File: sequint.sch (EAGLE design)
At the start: 66 parts, among them IC1 STM32F10XCXT6, Q1 MOSFET-NCHANNELSMD, Q2 MOSFET-NCHANNELSMD, Q3 MOSFET-NCHANNELSMD, Q4 MOSFET-NCHANNELSMD, Q5 16MHz, U1 LSM330DLCTRLGA, U2 MCP73831, U4 NRF24L01SMD

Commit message: s/trace antenna/chip antenna/, passes DRC.
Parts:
- removed ANT1: ANTENNA, adafruit:ANTENNA
- added U$1: ANTENNA2SMD5, SparkFun-RF:ANTENNA2SMD5
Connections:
- net ANT: now also U$1.SIGNAL; no longer ANT1.FEED
- net GND: no longer ANT1.GND
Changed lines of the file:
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@@
 <part name="GND7" library="SparkFun" deviceset="GND" device=""/>
 <part name="U4" library="SparkFun" deviceset="NRF24L01" device="SMD"/>
-<part name="ANT1" library="adafruit" deviceset="ANTENNA" device=""/>
 <part name="JPRF-A" library="nonolith" deviceset="HEADER-1X4" device="ROUND"/>
 <part name="JPRF-B" library="nonolith" deviceset="HEADER-1X4" device="ROUND"/>
@@
 <part name="R10" library="nonolith" deviceset="RESISTOR" device="0603" value="130o"/>
 <part name="JP1" library="nonolith" deviceset="HEADER-1X4" device="ROUND" value="PORTC"/>
+<part name="U$1" library="SparkFun-RF" deviceset="ANTENNA2" device="SMD5"/>
 </parts>
 <sheets>
@@
 <attribute name="VALUE" x="45.466" y="72.136" size="1.6764" layer="96"/>
 </instance>
-<instance part="ANT1" gate="G$1" x="111.76" y="88.9"/>
 <instance part="JPRF-A" gate="A" x="-10.16" y="78.74"/>
 <instance part="JPRF-B" gate="A" x="-7.62" y="81.28" rot="R180"/>
@@
 <instance part="C18" gate="G$1" x="96.52" y="22.86"/>
 <instance part="C19" gate="G$1" x="106.68" y="22.86"/>
+<instance part="U$1" gate="G$1" x="111.76" y="88.9"/>
 </instances>
 <busses>
@@
 <pinref part="C13" gate="G$1" pin="P$1"/>
 <pinref part="GND7" gate="1" pin="GND"/>
-<pinref part="ANT1" gate="G$1" pin="GND"/>
-<wire x1="114.3" y1="88.9" x2="114.3" y2="71.12" width="0" layer="91"/>
-<wire x1="114.3" y1="71.12" x2="101.6" y2="71.12" width="0" layer="91"/>
 </segment>
 <segment>
@@
 <wire x1="101.6" y1="81.28" x2="101.6" y2="83.82" width="0" layer="91"/>
 <wire x1="101.6" y1="83.82" x2="111.76" y2="83.82" width="0" layer="91"/>
-<wire x1="111.76" y1="83.82" x2="111.76" y2="88.9" width="0" layer="91"/>
 <junction x="101.6" y="83.82"/>
 <label x="104.14" y="83.82" size="1.778" layer="95"/>
 <pinref part="C14" gate="G$1" pin="P$2"/>
 <pinref part="C13" gate="G$1" pin="P$2"/>
-<pinref part="ANT1" gate="G$1" pin="FEED"/>
-</segment>
-</net>
+<pinref part="U$1" gate="G$1" pin="SIGNAL"/>
+</segment>
+</net>

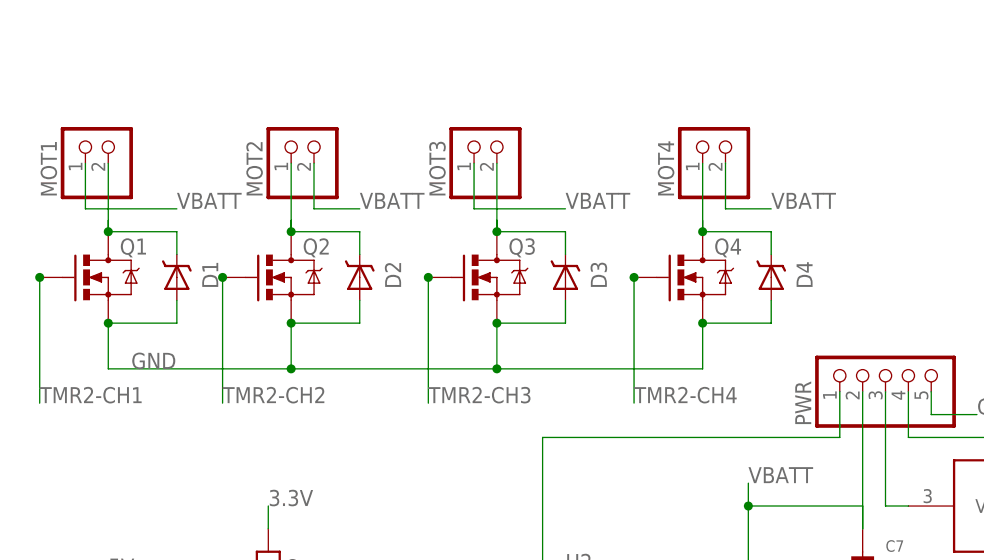
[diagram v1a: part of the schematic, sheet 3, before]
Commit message: removed fatty diodes, s/0603/0402/
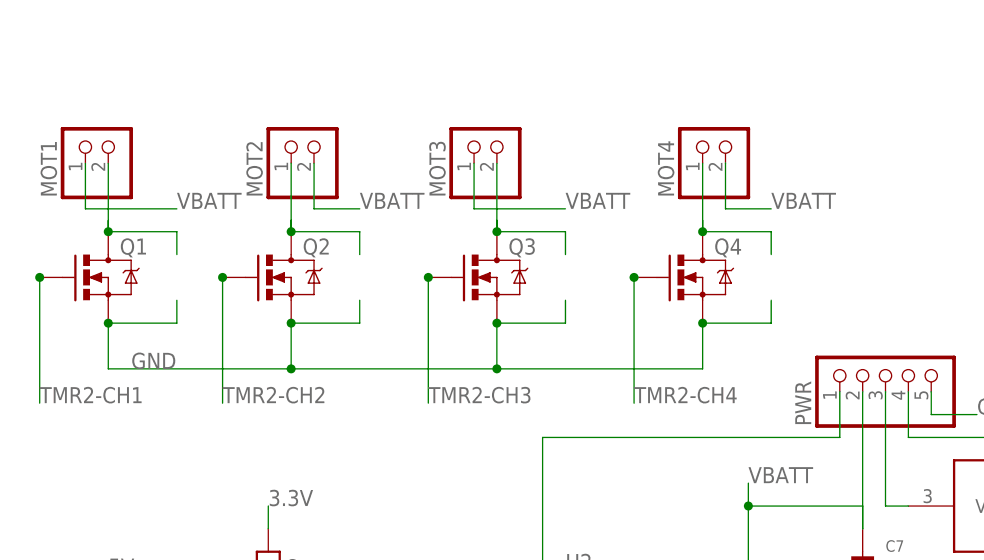
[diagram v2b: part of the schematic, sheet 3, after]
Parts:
- removed D1, D2, D3, D4: SCHOTTKY, nonolith:SCHOTTKY
- C1, C10, C11, C12, C13, C14, C15, C16, C17, C18, C19, C2, C21, C22, C3, C4, C5, C6, C8, C9: device nonolith:CAP_CERAMIC0603 -> nonolith:CAP_CERAMIC0402
- C20: device nonolith:CAP_CERAMIC1206 -> nonolith:CAP_CERAMIC0402
- L1, L2, L3: device SparkFun:INDUCTOR0603 -> SparkFun:INDUCTOR0402
- R1, R10, R2, R3, R4, R5, R6, R7, R8, R9: device nonolith:RESISTOR0603 -> nonolith:RESISTOR0402
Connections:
- net GND: no longer D1.A, D2.A, D3.A, D4.A
- net VL-1: no longer D1.C
- net VL-2: no longer D2.C
- net VL-3: no longer D3.C
- net VL-4: no longer D4.C

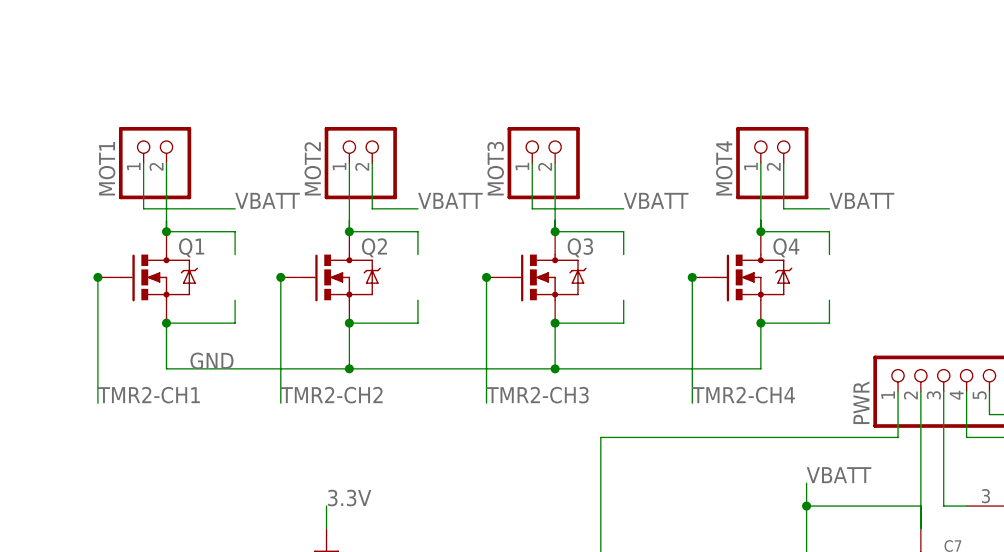
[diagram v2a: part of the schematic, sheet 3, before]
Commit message: added snubber diodes in SOD523 aka tiny
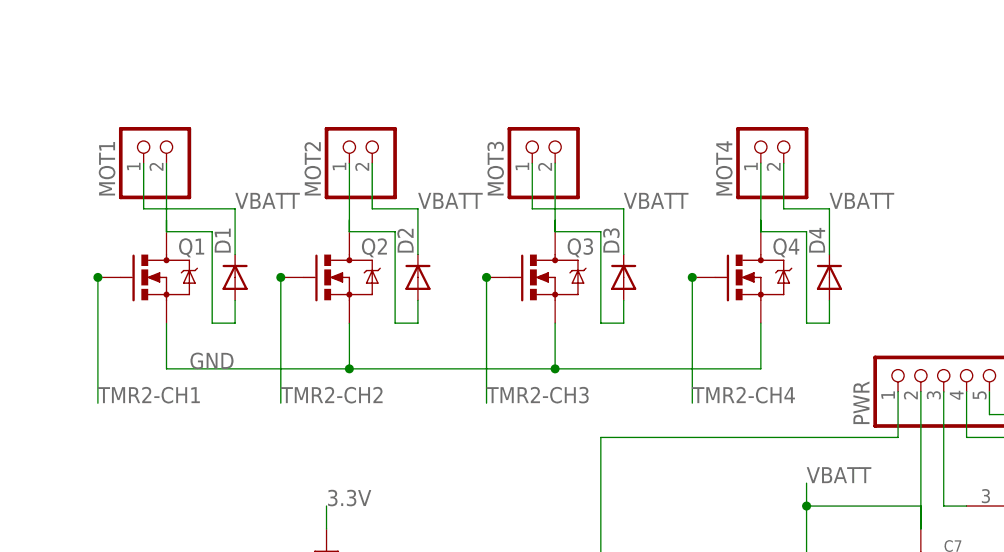
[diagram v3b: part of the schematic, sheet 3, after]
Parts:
- added D1, D2, D3, D4: (no value), SparkFun-DiscreteSemi:DIODESOD523
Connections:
- net VBATT: now also D1.C, D2.C, D3.C, D4.C
- net VL-1: now also D1.A
- net VL-2: now also D2.A
- net VL-3: now also D3.A
- net VL-4: now also D4.A
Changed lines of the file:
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@@
 <part name="JP1" library="nonolith" deviceset="HEADER-1X4" device="ROUND" value="PORTC"/>
 <part name="U$1" library="SparkFun-RF" deviceset="ANTENNA2" device="SMD5"/>
+<part name="D1" library="SparkFun-DiscreteSemi" deviceset="DIODE" device="SOD523"/>
+<part name="D2" library="SparkFun-DiscreteSemi" deviceset="DIODE" device="SOD523"/>
+<part name="D3" library="SparkFun-DiscreteSemi" deviceset="DIODE" device="SOD523"/>
+<part name="D4" library="SparkFun-DiscreteSemi" deviceset="DIODE" device="SOD523"/>
 </parts>
 <sheets>
@@
 <instance part="RN1" gate="C" x="149.86" y="66.04" rot="R90"/>
 <instance part="RN1" gate="D" x="149.86" y="50.8" rot="R90"/>
+<instance part="D1" gate="G$1" x="30.48" y="48.26" rot="R90"/>
+<instance part="D2" gate="G$1" x="50.8" y="48.26" rot="R90"/>
+<instance part="D3" gate="G$1" x="73.66" y="48.26" rot="R90"/>
+<instance part="D4" gate="G$1" x="96.52" y="48.26" rot="R90"/>
 </instances>
 <busses>
@@
 <segment>
 <pinref part="Q4" gate="G$1" pin="D"/>
-<wire x1="96.52" y1="50.8" x2="96.52" y2="53.34" width="0" layer="91"/>
-<wire x1="96.52" y1="53.34" x2="88.9" y2="53.34" width="0" layer="91"/>
 <wire x1="88.9" y1="53.34" x2="88.9" y2="54.61" width="0" layer="91"/>
-<junction x="88.9" y="53.34"/>
 <pinref part="MOT4" gate="G$1" pin="1"/>
 <wire x1="88.9" y1="53.34" x2="88.9" y2="60.96" width="0" layer="91"/>
+<wire x1="88.9" y1="53.34" x2="93.98" y2="53.34" width="0" layer="91"/>
+<wire x1="93.98" y1="53.34" x2="93.98" y2="43.18" width="0" layer="91"/>
+<pinref part="D4" gate="G$1" pin="A"/>
+<wire x1="96.52" y1="45.72" x2="96.52" y2="43.18" width="0" layer="91"/>
+<wire x1="93.98" y1="43.18" x2="96.52" y2="43.18" width="0" layer="91"/>
 </segment>
 </net>
@@
 <segment>
 <pinref part="Q3" gate="G$1" pin="D"/>
-<wire x1="73.66" y1="50.8" x2="73.66" y2="53.34" width="0" layer="91"/>
-<wire x1="73.66" y1="53.34" x2="66.04" y2="53.34" width="0" layer="91"/>
 <wire x1="66.04" y1="53.34" x2="66.04" y2="54.61" width="0" layer="91"/>
-<junction x="66.04" y="53.34"/>
 <pinref part="MOT3" gate="G$1" pin="2"/>
 <wire x1="66.04" y1="60.96" x2="66.04" y2="53.34" width="0" layer="91"/>
+<wire x1="66.04" y1="53.34" x2="71.12" y2="53.34" width="0" layer="91"/>
+<wire x1="71.12" y1="53.34" x2="71.12" y2="43.18" width="0" layer="91"/>
+<pinref part="D3" gate="G$1" pin="A"/>
+<wire x1="73.66" y1="45.72" x2="73.66" y2="43.18" width="0" layer="91"/>
+<wire x1="71.12" y1="43.18" x2="73.66" y2="43.18" width="0" layer="91"/>
 </segment>
 </net>
@@
 <segment>
 <pinref part="Q2" gate="G$1" pin="D"/>
-<wire x1="50.8" y1="50.8" x2="50.8" y2="53.34" width="0" layer="91"/>
-<wire x1="50.8" y1="53.34" x2="43.18" y2="53.34" width="0" layer="91"/>
 <wire x1="43.18" y1="53.34" x2="43.18" y2="54.61" width="0" layer="91"/>
-<junction x="43.18" y="53.34"/>
 <pinref part="MOT2" gate="G$1" pin="1"/>
 <wire x1="43.18" y1="60.96" x2="43.18" y2="53.34" width="0" layer="91"/>
+<wire x1="43.18" y1="53.34" x2="48.26" y2="53.34" width="0" layer="91"/>
+<wire x1="48.26" y1="53.34" x2="48.26" y2="43.18" width="0" layer="91"/>
+<pinref part="D2" gate="G$1" pin="A"/>
+<wire x1="50.8" y1="45.72" x2="50.8" y2="43.18" width="0" layer="91"/>
+<wire x1="48.26" y1="43.18" x2="50.8" y2="43.18" width="0" layer="91"/>
 </segment>
 </net>
@@
 <segment>
 <pinref part="Q1" gate="G$1" pin="D"/>
-<wire x1="30.48" y1="50.8" x2="30.48" y2="53.34" width="0" layer="91"/>
-<wire x1="30.48" y1="53.34" x2="22.86" y2="53.34" width="0" layer="91"/>
 <wire x1="22.86" y1="53.34" x2="22.86" y2="54.61" width="0" layer="91"/>
-<junction x="22.86" y="53.34"/>
 <pinref part="MOT1" gate="G$1" pin="2"/>
 <wire x1="22.86" y1="53.34" x2="22.86" y2="60.96" width="0" layer="91"/>
+<wire x1="22.86" y1="53.34" x2="27.94" y2="53.34" width="0" layer="91"/>
+<wire x1="27.94" y1="53.34" x2="27.94" y2="43.18" width="0" layer="91"/>
+<pinref part="D1" gate="G$1" pin="A"/>
+<wire x1="30.48" y1="45.72" x2="30.48" y2="43.18" width="0" layer="91"/>
+<wire x1="27.94" y1="43.18" x2="30.48" y2="43.18" width="0" layer="91"/>
 </segment>
 </net>
@@
 <wire x1="66.04" y1="38.1" x2="88.9" y2="38.1" width="0" layer="91"/>
 <wire x1="88.9" y1="38.1" x2="88.9" y2="43.18" width="0" layer="91"/>
-<wire x1="30.48" y1="45.72" x2="30.48" y2="43.18" width="0" layer="91"/>
-<wire x1="30.48" y1="43.18" x2="22.86" y2="43.18" width="0" layer="91"/>
-<wire x1="50.8" y1="45.72" x2="50.8" y2="43.18" width="0" layer="91"/>
-<wire x1="50.8" y1="43.18" x2="43.18" y2="43.18" width="0" layer="91"/>
-<wire x1="73.66" y1="45.72" x2="73.66" y2="43.18" width="0" layer="91"/>
-<wire x1="73.66" y1="43.18" x2="66.04" y2="43.18" width="0" layer="91"/>
-<wire x1="96.52" y1="45.72" x2="96.52" y2="43.18" width="0" layer="91"/>
-<wire x1="96.52" y1="43.18" x2="88.9" y2="43.18" width="0" layer="91"/>
-<junction x="22.86" y="43.18"/>
-<junction x="43.18" y="43.18"/>
-<junction x="66.04" y="43.18"/>
-<junction x="88.9" y="43.18"/>
 <junction x="66.04" y="38.1"/>
 <junction x="43.18" y="38.1"/>
@@
 <label x="30.48" y="55.88" size="1.778" layer="95"/>
 <pinref part="MOT1" gate="G$1" pin="1"/>
+<wire x1="30.48" y1="50.8" x2="30.48" y2="55.88" width="0" layer="91"/>
 <wire x1="30.48" y1="55.88" x2="20.32" y2="55.88" width="0" layer="91"/>
 <wire x1="20.32" y1="55.88" x2="20.32" y2="60.96" width="0" layer="91"/>
+<pinref part="D1" gate="G$1" pin="C"/>
 </segment>
 <segment>
@@
 <wire x1="45.72" y1="55.88" x2="50.8" y2="55.88" width="0" layer="91"/>
 <label x="50.8" y="55.88" size="1.778" layer="95"/>
+<pinref part="D2" gate="G$1" pin="C"/>
+<wire x1="50.8" y1="50.8" x2="50.8" y2="55.88" width="0" layer="91"/>
 </segment>
 <segment>
 <label x="73.66" y="55.88" size="1.778" layer="95"/>
 <pinref part="MOT3" gate="G$1" pin="1"/>
+<wire x1="73.66" y1="50.8" x2="73.66" y2="55.88" width="0" layer="91"/>
 <wire x1="73.66" y1="55.88" x2="63.5" y2="55.88" width="0" layer="91"/>
 <wire x1="63.5" y1="55.88" x2="63.5" y2="60.96" width="0" layer="91"/>
+<pinref part="D3" gate="G$1" pin="C"/>
 </segment>
 <segment>
@@
 <wire x1="91.44" y1="55.88" x2="96.52" y2="55.88" width="0" layer="91"/>
 <label x="96.52" y="55.88" size="1.778" layer="95"/>
-</segment>
-<segment>
+<pinref part="D4" gate="G$1" pin="C"/>
+<wire x1="96.52" y1="50.8" x2="96.52" y2="55.88" width="0" layer="91"/>
+</segment>
+<segment>

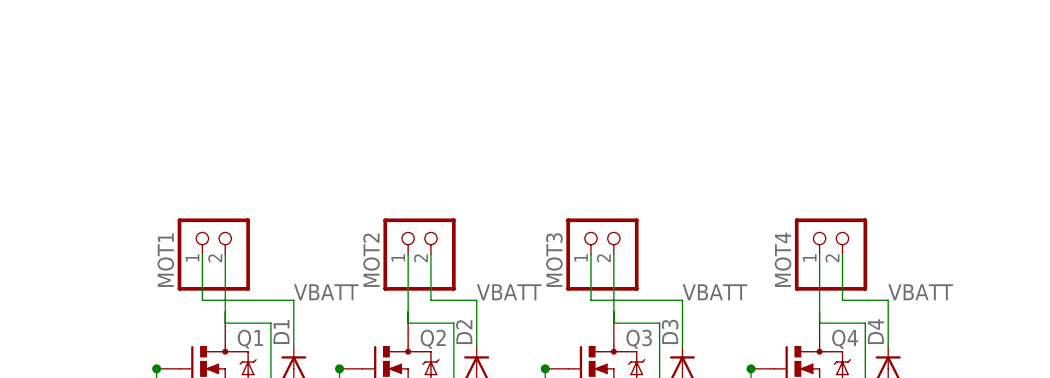
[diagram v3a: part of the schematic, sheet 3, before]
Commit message: Add servo headers
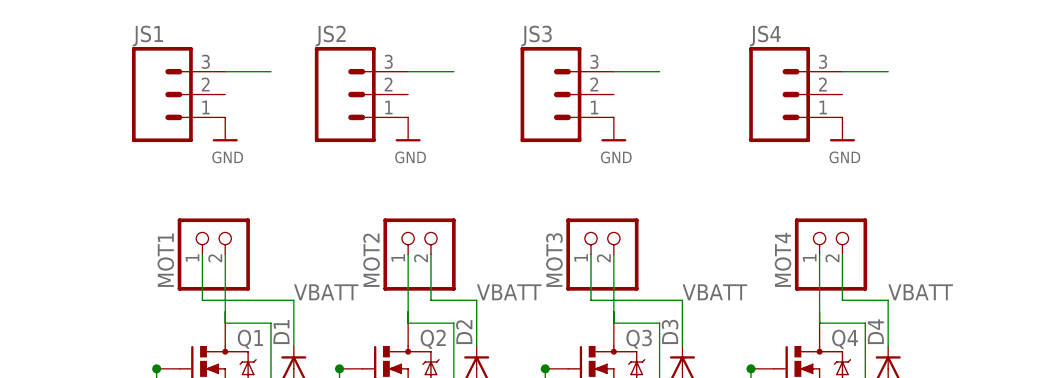
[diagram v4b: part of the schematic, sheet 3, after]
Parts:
- added JS1, JS2, JS3, JS4: (no value), SparkFun:M03LOCK
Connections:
- net GND: now also JS1.1, JS2.1, JS3.1, JS4.1
- net TMR2-CH1: now also JS1.3
- net TMR2-CH2: now also JS2.3
- net TMR2-CH3: now also JS3.3
- net TMR2-CH4: now also JS4.3

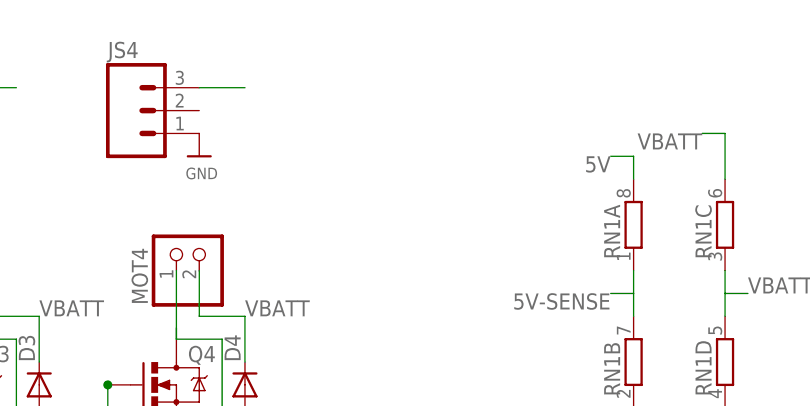
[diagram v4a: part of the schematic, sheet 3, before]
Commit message: Add test motor footprint
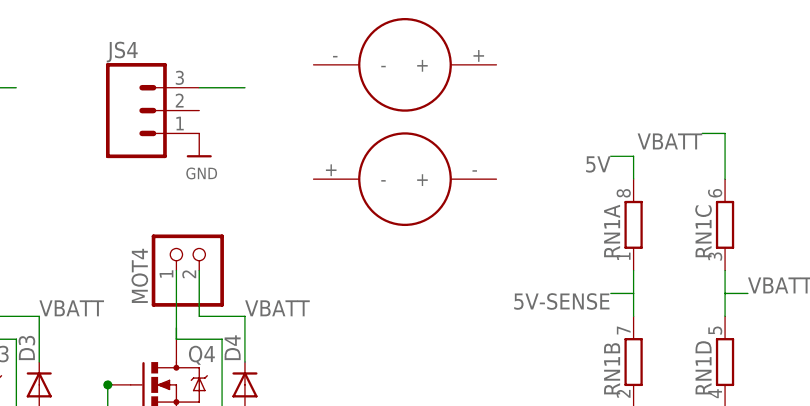
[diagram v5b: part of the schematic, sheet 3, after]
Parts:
- added U$6: MOT_RICCW, nonolith:MOT_RICCW
- added U$7: MOT_RICCCW, nonolith:MOT_RICCCW
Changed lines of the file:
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@@
 <part name="U$4" library="nonolith" deviceset="GND" device=""/>
 <part name="U$5" library="nonolith" deviceset="GND" device=""/>
+<part name="U$6" library="nonolith" deviceset="MOT_RIC" device="CW"/>
+<part name="U$7" library="nonolith" deviceset="MOT_RIC" device="CCW"/>
 </parts>
 <sheets>
@@
 <instance part="U$4" gate="G$1" x="66.04" y="73.66"/>
 <instance part="U$5" gate="G$1" x="91.44" y="73.66"/>
+<instance part="U$6" gate="G$1" x="129.54" y="78.74"/>
+<instance part="U$7" gate="G$1" x="129.54" y="66.04"/>
 </instances>
 <busses>

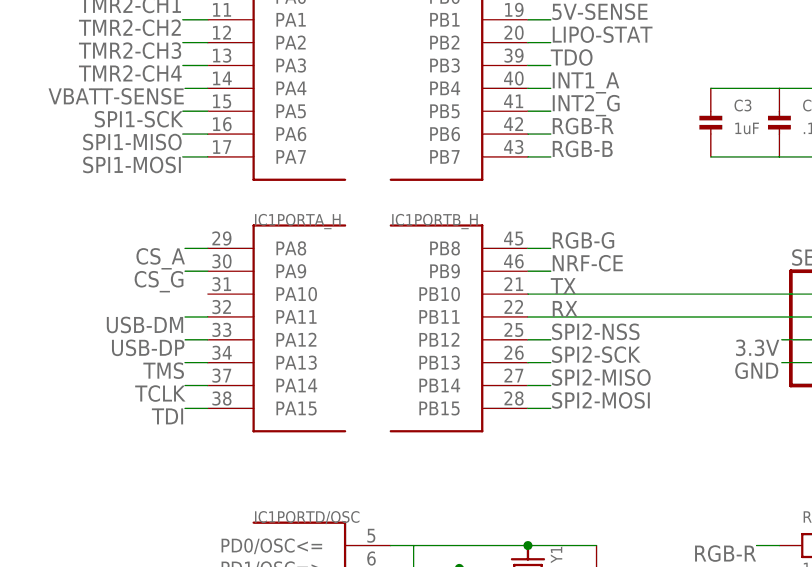
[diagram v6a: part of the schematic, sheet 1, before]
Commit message: Move nrf-ce to pin 31 for better routing
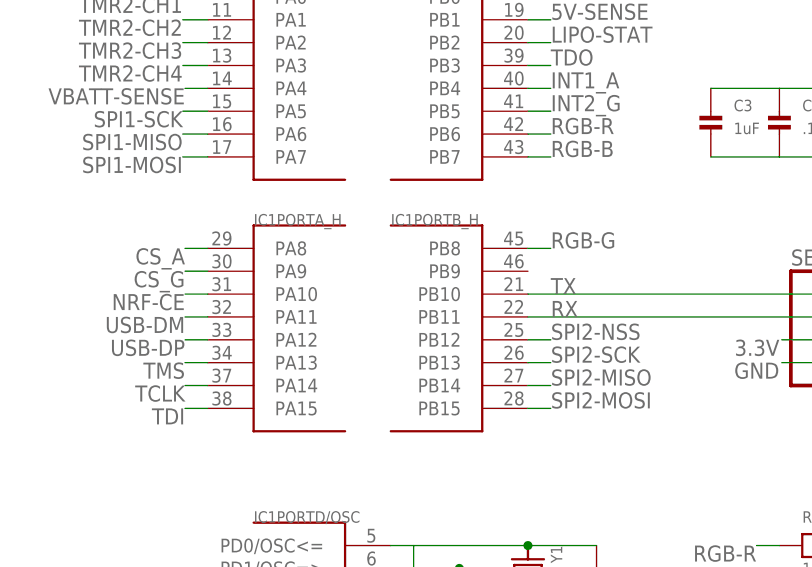
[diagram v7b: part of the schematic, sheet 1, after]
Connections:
- net NRF-CE: now also IC1PORTA_H.PA10; no longer IC1PORTB_H.PB9
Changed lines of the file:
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@@
 <net name="NRF-CE" class="0">
 <segment>
-<label x="33.02" y="73.66" size="1.778" layer="95"/>
-<pinref part="IC1" gate="PORTB_H" pin="PB9"/>
-<wire x1="30.48" y1="73.66" x2="33.02" y2="73.66" width="0" layer="91"/>
+<pinref part="IC1" gate="PORTA_H" pin="PA10"/>
+<wire x1="-5.08" y1="71.12" x2="-7.62" y2="71.12" width="0.0254" layer="91"/>
+<label x="-7.62" y="71.12" size="1.778" layer="95" rot="R180"/>
 </segment>
 </net>
